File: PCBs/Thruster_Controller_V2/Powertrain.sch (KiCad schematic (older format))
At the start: 53 parts, among them Q1 SIZF906DT, Q2 SIZF906DT, Q3 SIZF906DT, U1 DRV8305

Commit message: Powertrain Schematic
- Updated PT schematic, footprints, and part numbers.
- Big change is moving from the DRV8305 to the DRV8320S
- BIG space and cost savings!!
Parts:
- removed C12, C14, C31: 22uF, Capacitors_SMD:C_1206, symbol Device:C
- removed C16, C18, C9: 1000pF, Capacitors_SMD:C_0402, symbol Device:C_Small
- removed C19: 2.2uF, Capacitors_SMD:C_0603, symbol Device:C_Small
- removed C27, C3: 1uF, Capacitors_SMD:C_0603, symbol Device:C_Small
- removed C4: 0.047uF, Capacitors_SMD:C_0402, symbol Device:C_Small
- removed R1: 10k, Resistors_SMD:R_0603, symbol Device:R_US
- removed R2: 100, Resistors_SMD:R_0603, symbol Device:R_US
- removed U1: DRV8305, Thruster_Controller:DRV8305, symbol ESC_Drivetrain_V1:DRV8305
- added C?: 0.1uF, Capacitors_SMD:C_0402, symbol Device:C_Small
- added C? (x3): 0.01uF, Capacitors_SMD:C_0402, symbol Device:C_Small
- added R?: 56, Resistors_SMD:R_0402, symbol Device:R_US
- added R? (x3): 2.49k, Resistors_SMD:R_0402, symbol Device:R_US
- added R? (x3): 27.4k, Resistors_SMD:R_0402, symbol Device:R_US
- added R?: 2.2k, Resistors_SMD:R_0402, symbol Device:R_Small_US
- added U?: DRV8320S, Housings_DFN_QFN:WQFN-32-1EP_5x5mm_Pitch0.5mm, symbol Thruster_Controller:DRV8320S
- C10, C13, C15: value 22uF -> 220uF
- Q1, Q2, Q3: symbol ESC_Drivetrain_V1:SIZF906DT -> Thruster_Controller:SIZF906DT
- R10: footprint Resistors_SMD:R_0805 -> Resistors_SMD:R_0603; Digikey 2019-RK73B2ATTD331JCT-ND -> RMCF0603JT330RCT-ND
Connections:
- net SN1 is gone; now on net SPA: NT6.1
- net SN2 is gone; now on net SPB: NT4.1
- net SN3 is gone; now on net SPC: NT5.1
- net SP2 is gone; now on net SNA: NT1.1
- net SP3 is gone; now on net SNA: NT2.1
- net +3V3: now also R?.1
- net +BATT: now also C5.1, C?.1, C?.1, C?.1, C?.1, U?.3 (VM), U?.4 (VDRAIN)
- net EN_GATE: now also U?.22 (EN_GATE)
- net GH_A: now also U?.5 (GHA)
- net GH_B: now also U?.12 (GHB)
- net GH_C: now also U?.13 (GHC)
- net GL_A: now also U?.7 (GLA)
- net GL_B: now also U?.10 (GLB)
- net GL_C: now also U?.15 (GLC)
- net GND: now also C?.2, U?.23 (AGND), U?.31 (PGND), U?.33 (PAD); no longer C24.2, C25.2, C26.2, C5.2
- net INH_A: now also U?.25 (INHA)
- net INH_B: now also U?.27 (INHB)
- net INH_C: now also U?.29 (INHC)
- net INL_A: now also U?.26 (INLA)
- net INL_B: now also U?.28 (INLB)
- net INL_C: now also U?.30 (INLC)
- net ISEN_A: now also R?.1, R?.2; no longer C24.1, R20.2
- net ISEN_B: now also R?.1, R?.2; no longer C25.1, R21.2
- net ISEN_C: now also R?.1, R?.2; no longer C26.1, R22.2
- net SH_A: now also U?.6 (SHA)
- net SH_B: now also U?.11 (SHB)
- net SH_C: now also U?.14 (SHC)
- net SL_A: now also C?.2, U?.8 (SLA)
- net SL_B: now also C?.2, U?.9 (SLB)
- net SL_C: now also C?.2, U?.16 (SLC)
- net SPI_CLK: now also U?.20 (SCLK)
- net SPI_CS_0: now also U?.21 (~SCS~)
- net SPI_MISO: now also R?.2, U?.18 (SDO)
- net SPI_MOSI: now also U?.19 (SDI)
- net nFAULT: now also U?.17 (~FAULT~)
- net at C20.1: now also U?.24 (DVDD)
- net at C2.1: now also U?.32 (CPL)
- net at C2.2: now also U?.1 (CPH)
- net ISEN_A_DRV renamed SPA
- net ISEN_B_DRV renamed SPB
- net ISEN_C_DRV renamed SPC
- net SP1 renamed SNA
- net SNA: now also R?.1
- new net: C26.1, R22.2, R?.1
- new net: C24.1, R20.2, R?.1
- new net: C5.2, U?.2 (VCP)
- new net: C25.1, R21.2, R?.1
- new net DAC: R?.2, R?.2, R?.2
- new net PGA_GND: C24.2, C25.2, C26.2, R?.2
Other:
- note added: "DRV8320S"
- note removed: "Can stack additional ceramic caps"
- note removed: "Ceramic Cap Decoupling Bank"
- note removed: "DRV8305"
- note removed: "Digikey Options:\n1. 565-APXJ160ARA221MF61GCT-ND\n2. 565-4528-1-ND\n3. P16498CT-ND"
- moved on the sheet: C1, C10, C13, C15, C2, C20, C24, C25, C26, C5, C7, D2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

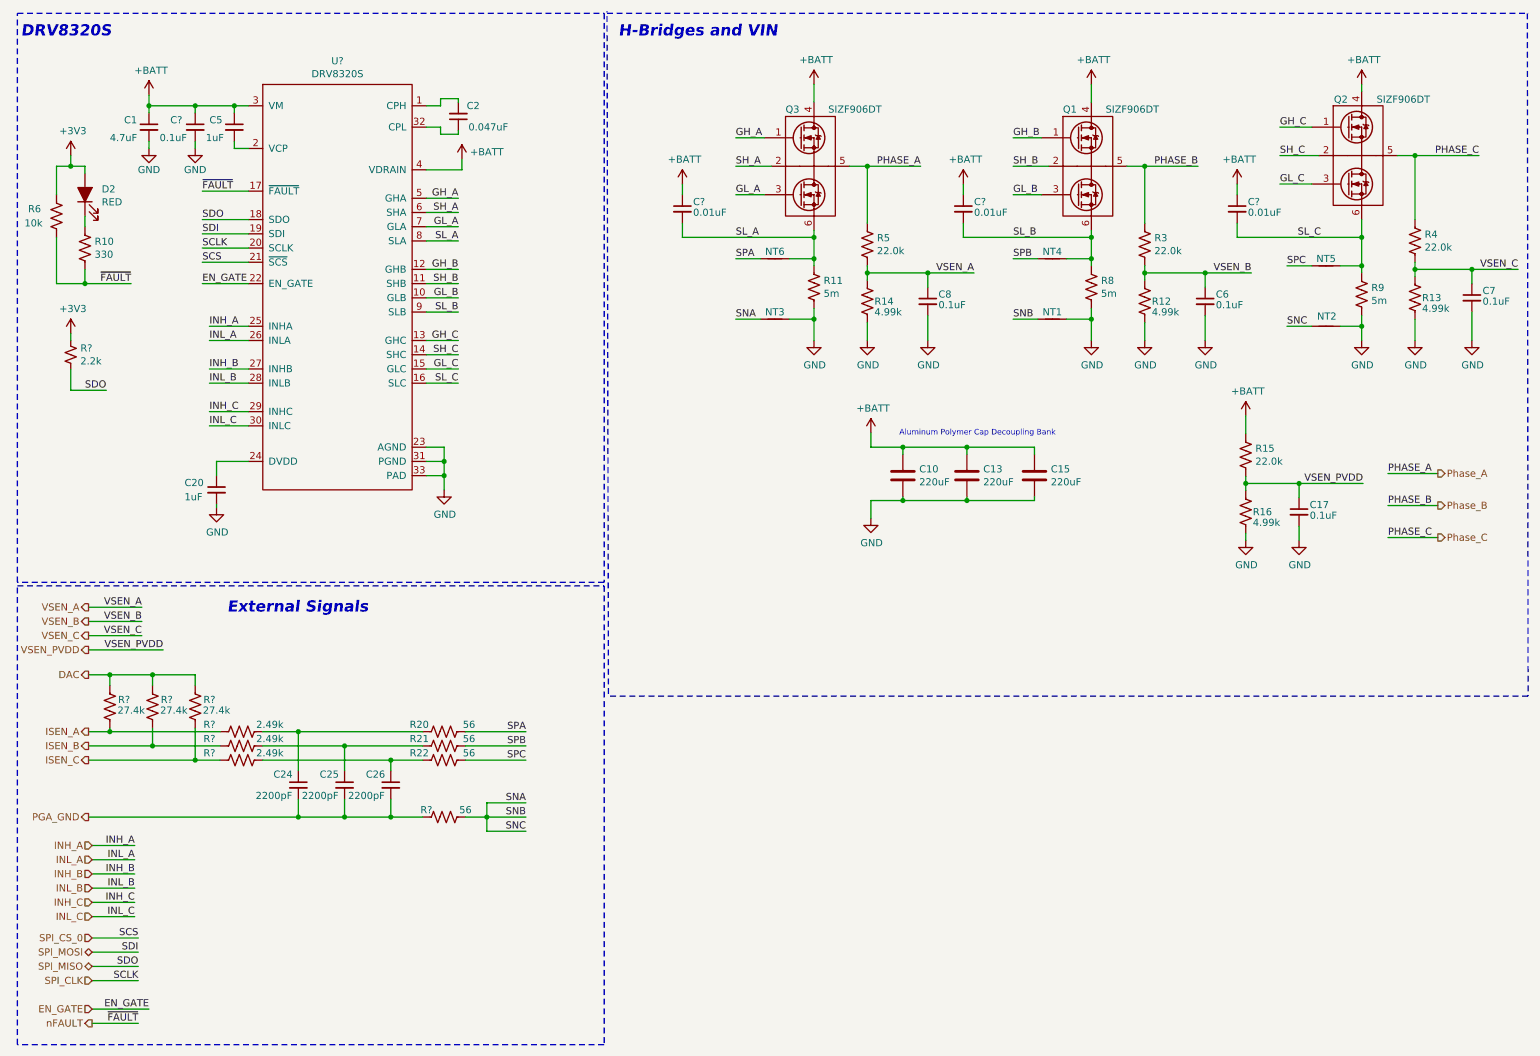
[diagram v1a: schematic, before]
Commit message: Schematic V1
- Completed New Schematic
_ Multiplexed all required signals, may need to redo some arrangments to aid in routing, just because I can and already have to reassign all pins in the SW.
- Created new BOM, only $1 more expensive per board, still might be able to lower that further.
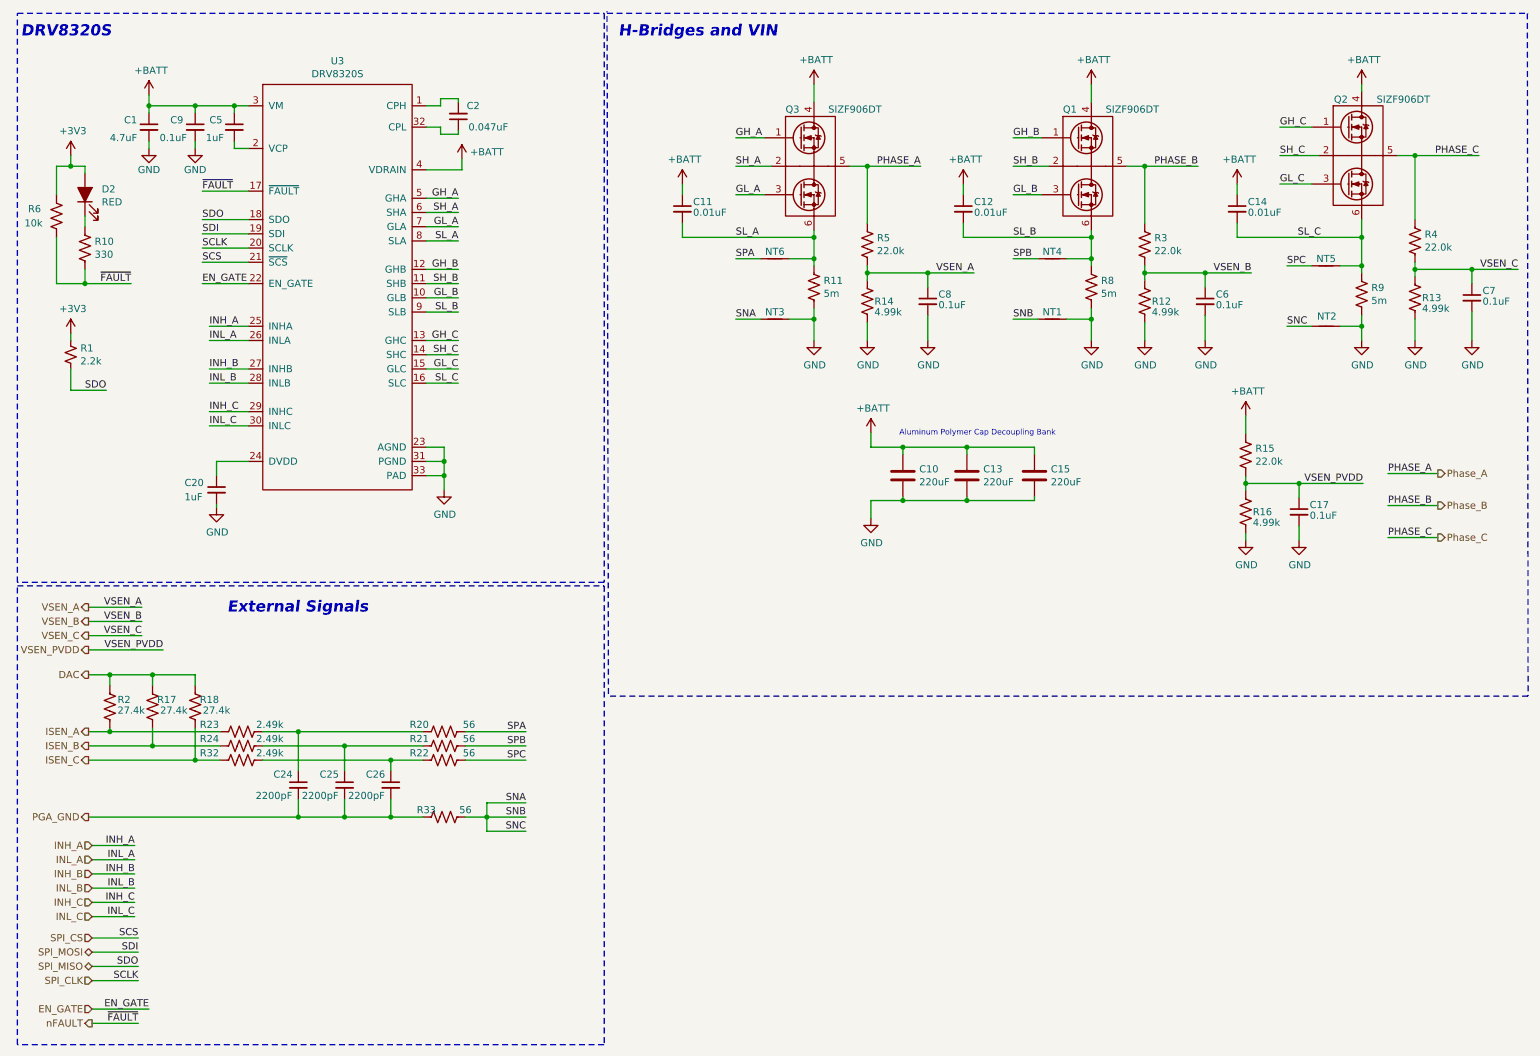
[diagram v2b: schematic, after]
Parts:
- R6: footprint Resistors_SMD:R_0603 -> Resistors_SMD:R_0402; Digikey RMCF0603JT10K0CT-ND -> 2019-RK73B1ETTP103JCT-ND
- gave numbers to parts that had none: 13
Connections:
- net SPI_CS_0 renamed SPI_CS
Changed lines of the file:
@@
 $Descr A4 11693 8268
 encoding utf-8
-Sheet 3 3
+Sheet 2 3
 Title "Powertrain"
 Date "2020-01-16"
@@
 F 0 "R6" H 575 1975 50  0000 L CNN
 F 1 "10k" H 550 1875 50  0000 L CNN
-F 2 "Resistors_SMD:R_0603" V 815 1915 50  0001 C CNN
+F 2 "Resistors_SMD:R_0402" V 815 1915 50  0001 C CNN
 F 3 "~" H 775 1925 50  0001 C CNN
-F 4 "RMCF0603JT10K0CT-ND" H 775 1925 50  0001 C CNN "Digikey"
+F 4 "2019-RK73B1ETTP103JCT-ND" H 775 1925 50  0001 C CNN "Digikey"
 	1    775  1925
 	1    0    0    -1
@@
 	1025 6850 1325 6850
 Text HLabel 1025 7000 0    50   Input ~ 0
-SPI_CS_0
+SPI_CS
 Text HLabel 1025 7100 0    50   BiDi ~ 0
 SPI_MOSI
@@
 	10325 1500 10775 1500
 $Comp
-L Thruster_Controller:DRV8320S U?
+L Thruster_Controller:DRV8320S U3
 U 1 1 5F055F39
 P 2775 3350
-F 0 "U?" H 2750 5865 50  0000 C CNN
+F 0 "U3" H 2750 5865 50  0000 C CNN
 F 1 "DRV8320S" H 2750 5774 50  0000 C CNN
 F 2 "Housings_DFN_QFN:WQFN-32-1EP_5x5mm_Pitch0.5mm" H 2675 4000 79  0001 C CNN
@@
 Connection ~ 6725 3925
 $Comp
-L power:GND #PWR?
+L power:GND #PWR0114
 U 1 1 5F1F0E7D
 P 6500 4050
-F 0 "#PWR?" H 6500 3800 50  0001 C CNN
+F 0 "#PWR0114" H 6500 3800 50  0001 C CNN
 F 1 "GND" H 6505 3877 50  0000 C CNN
 F 2 "" H 6500 4050 50  0001 C CNN
@@
 	1425 1400 1425 1450
 $Comp
-L power:GND #PWR?
+L power:GND #PWR0117
 U 1 1 5F2B60E2
 P 1425 1450
-F 0 "#PWR?" H 1425 1200 50  0001 C CNN
+F 0 "#PWR0117" H 1425 1200 50  0001 C CNN
 F 1 "GND" H 1425 1300 50  0000 C CNN
 F 2 "" H 1425 1450 50  0001 C CNN
@@
 $EndComp
 $Comp
-L Device:C_Small C?
+L Device:C_Small C9
 U 1 1 5F2CB787
 P 1750 1300
-F 0 "C?" H 1575 1350 50  0000 L CNN
+F 0 "C9" H 1575 1350 50  0000 L CNN
 F 1 "0.1uF" H 1500 1225 50  0000 L CNN
 F 2 "Capacitors_SMD:C_0402" H 1750 1300 50  0001 C CNN
@@
 	1750 1400 1750 1450
 $Comp
-L power:GND #PWR?
+L power:GND #PWR0118
 U 1 1 5F2FCED2
 P 1750 1450
-F 0 "#PWR?" H 1750 1200 50  0001 C CNN
+F 0 "#PWR0118" H 1750 1200 50  0001 C CNN
 F 1 "GND" H 1750 1300 50  0000 C CNN
 F 2 "" H 1750 1450 50  0001 C CNN
@@
 $EndComp
 $Comp
-L Device:C_Small C?
+L Device:C_Small C11
 U 1 1 5F2FF0BC
 P 5175 1875
-F 0 "C?" H 5250 1925 50  0000 L CNN
+F 0 "C11" H 5250 1925 50  0000 L CNN
 F 1 "0.01uF" H 5250 1850 50  0000 L CNN
 F 2 "Capacitors_SMD:C_0402" H 5175 1875 50  0001 C CNN
@@
 $EndComp
 $Comp
-L Device:C_Small C?
+L Device:C_Small C12
 U 1 1 5F30094C
 P 7150 1875
-F 0 "C?" H 7225 1925 50  0000 L CNN
+F 0 "C12" H 7225 1925 50  0000 L CNN
 F 1 "0.01uF" H 7225 1850 50  0000 L CNN
 F 2 "Capacitors_SMD:C_0402" H 7150 1875 50  0001 C CNN
@@
 $EndComp
 $Comp
-L Device:C_Small C?
+L Device:C_Small C14
 U 1 1 5F301F05
 P 9075 1875
-F 0 "C?" H 9150 1925 50  0000 L CNN
+F 0 "C14" H 9150 1925 50  0000 L CNN
 F 1 "0.01uF" H 9150 1850 50  0000 L CNN
 F 2 "Capacitors_SMD:C_0402" H 9075 1875 50  0001 C CNN
@@
 $EndComp
 $Comp
-L power:+BATT #PWR?
+L power:+BATT #PWR0119
 U 1 1 5F3175C2
 P 9075 1700
-F 0 "#PWR?" H 9075 1550 50  0001 C CNN
+F 0 "#PWR0119" H 9075 1550 50  0001 C CNN
 F 1 "+BATT" H 9090 1873 50  0000 C CNN
 F 2 "" H 9075 1700 50  0001 C CNN
@@
 	7150 1775 7150 1700
 $Comp
-L power:+BATT #PWR?
+L power:+BATT #PWR0120
 U 1 1 5F34997A
 P 7150 1700
-F 0 "#PWR?" H 7150 1550 50  0001 C CNN
+F 0 "#PWR0120" H 7150 1550 50  0001 C CNN
 F 1 "+BATT" H 7165 1873 50  0000 C CNN
 F 2 "" H 7150 1700 50  0001 C CNN
@@
 	5175 1775 5175 1700
 $Comp
-L power:+BATT #PWR?
+L power:+BATT #PWR0122
 U 1 1 5F35EB2D
 P 5175 1700
-F 0 "#PWR?" H 5175 1550 50  0001 C CNN
+F 0 "#PWR0122" H 5175 1550 50  0001 C CNN
 F 1 "+BATT" H 5190 1873 50  0000 C CNN
 F 2 "" H 5175 1700 50  0001 C CNN
@@
 	9375 1500 9650 1500
 $Comp
-L Device:R_US R?
+L Device:R_US R33
 U 1 1 5F4AD0F5
 P 3500 6150
-F 0 "R?" V 3450 6025 50  0000 C CNN
+F 0 "R33" V 3450 6025 50  0000 C CNN
 F 1 "56" V 3450 6300 50  0000 C CNN
 F 2 "Resistors_SMD:R_0402" V 3540 6140 50  0001 C CNN
@@
 SPC
 $Comp
-L Device:R_US R?
+L Device:R_US R23
 U 1 1 5F555C48
 P 2075 5550
-F 0 "R?" V 2025 5325 50  0000 C CNN
+F 0 "R23" V 2025 5325 50  0000 C CNN
 F 1 "2.49k" V 2025 5750 50  0000 C CNN
 F 2 "Resistors_SMD:R_0402" V 2115 5540 50  0001 C CNN
@@
 $EndComp
 $Comp
-L Device:R_US R?
+L Device:R_US R24
 U 1 1 5F564237
 P 2075 5650
-F 0 "R?" V 2025 5425 50  0000 C CNN
+F 0 "R24" V 2025 5425 50  0000 C CNN
 F 1 "2.49k" V 2025 5850 50  0000 C CNN
 F 2 "Resistors_SMD:R_0402" V 2115 5640 50  0001 C CNN
@@
 $EndComp
 $Comp
-L Device:R_US R?
+L Device:R_US R32
 U 1 1 5F56455C
 P 2075 5750
-F 0 "R?" V 2025 5525 50  0000 C CNN
+F 0 "R32" V 2025 5525 50  0000 C CNN
 F 1 "2.49k" V 2025 5950 50  0000 C CNN
 F 2 "Resistors_SMD:R_0402" V 2115 5740 50  0001 C CNN
@@
 $EndComp
 $Comp
-L Device:R_US R?
+L Device:R_US R18
 U 1 1 5F57E485
 P 1750 5375
-F 0 "R?" H 1650 5325 50  0000 C CNN
+F 0 "R18" H 1650 5325 50  0000 C CNN
 F 1 "27.4k" H 1600 5400 50  0000 C CNN
 F 2 "Resistors_SMD:R_0402" V 1790 5365 50  0001 C CNN
@@
 Connection ~ 1150 5150
 $Comp
-L Device:R_US R?
+L Device:R_US R17
 U 1 1 5F64AD7E
 P 1450 5375
-F 0 "R?" H 1350 5325 50  0000 C CNN
+F 0 "R17" H 1350 5325 50  0000 C CNN
 F 1 "27.4k" H 1300 5400 50  0000 C CNN
 F 2 "Resistors_SMD:R_0402" V 1490 5365 50  0001 C CNN
@@
 $EndComp
 $Comp
-L Device:R_US R?
+L Device:R_US R2
 U 1 1 5F64B745
 P 1150 5375
-F 0 "R?" H 1050 5325 50  0000 C CNN
+F 0 "R2" H 1050 5325 50  0000 C CNN
 F 1 "27.4k" H 1000 5400 50  0000 C CNN
 F 2 "Resistors_SMD:R_0402" V 1190 5365 50  0001 C CNN
@@
 P 875 2900
 AR Path="/5E20A372/5F7CA226" Ref="R?"  Part="1"
-AR Path="/5E20A2BB/5F7CA226" Ref="R?"  Part="1"
-F 0 "R?" H 943 2946 50  0000 L CNN
+AR Path="/5E20A2BB/5F7CA226" Ref="R1"  Part="1"
+F 0 "R1" H 943 2946 50  0000 L CNN
 F 1 "2.2k" H 943 2855 50  0000 L CNN
 F 2 "Resistors_SMD:R_0402" H 875 2900 50  0001 C CNN
@@
 	875  3150 875  3000
 $Comp
-L power:+3V3 #PWR?
+L power:+3V3 #PWR0123
 U 1 1 5F7F5888
 P 875 2750
-F 0 "#PWR?" H 875 2600 50  0001 C CNN
+F 0 "#PWR0123" H 875 2600 50  0001 C CNN
 F 1 "+3V3" H 890 2923 50  0000 C CNN
 F 2 "" H 875 2750 50  0001 C CNN
